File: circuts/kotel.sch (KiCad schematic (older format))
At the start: 21 parts, among them IC1 ATMEGA328P-TQFP32, P1 Power, P2 RELE CONNECTOR, P3 UART_RST, P4 TWI SW, Q1 MOS_N, U1 MAX6634, U2 7805, X1 12mHz

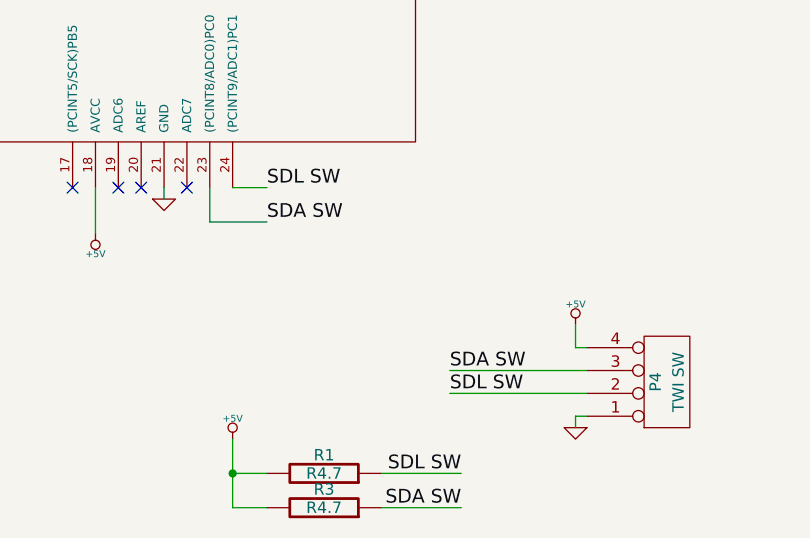
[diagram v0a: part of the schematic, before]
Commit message: Fixed software SDL/SCL.
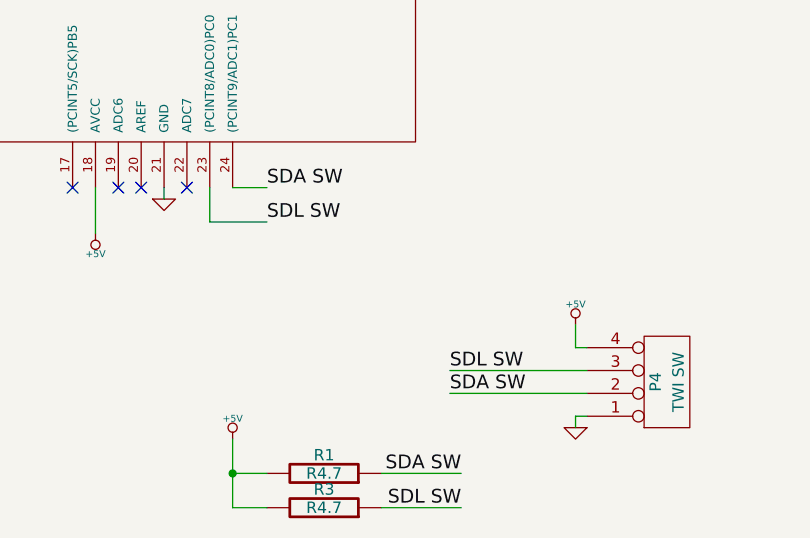
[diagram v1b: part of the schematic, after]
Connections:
- net SDA SW: now also IC1.24 ((PCINT9/ADC1)PC1), P4.2 (P2), R1.1; no longer IC1.23 ((PCINT8/ADC0)PC0), P4.3 (P3), R3.1
- net SDL SW: now also IC1.23 ((PCINT8/ADC0)PC0), P4.3 (P3), R3.1; no longer IC1.24 ((PCINT9/ADC1)PC1), P4.2 (P2), R1.1
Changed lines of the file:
@@
 Sheet 1 1
 Title "Humidity switcher"
-Date "26 sep 2013"
-Rev "v0.1"
+Date "6 oct 2013"
+Rev "v0.2"
 Comp ""
 Comment1 ""
@@
 $EndComp
 $Comp
-L GND #PWR018
+L GND #PWR017
 U 1 1 52360A3E
 P 6400 1550
-F 0 "#PWR018" H 6400 1550 30  0001 C CNN
+F 0 "#PWR017" H 6400 1550 30  0001 C CNN
 F 1 "GND" H 6400 1480 30  0001 C CNN
 F 2 "" H 6400 1550 60  0001 C CNN
@@
 $EndComp
 $Comp
-L GND #PWR019
+L GND #PWR018
 U 1 1 52360BDB
 P 2400 4950
-F 0 "#PWR019" H 2400 4950 30  0001 C CNN
+F 0 "#PWR018" H 2400 4950 30  0001 C CNN
 F 1 "GND" H 2400 4880 30  0001 C CNN
 F 2 "" H 2400 4950 60  0001 C CNN
@@
 $EndComp
 $Comp
-L +5V #PWR020
+L +5V #PWR019
 U 1 1 52360BE1
 P 2950 4400
-F 0 "#PWR020" H 2950 4490 20  0001 C CNN
+F 0 "#PWR019" H 2950 4490 20  0001 C CNN
 F 1 "+5V" H 2950 4490 30  0000 C CNN
 F 2 "" H 2950 4400 60  0000 C CNN
@@
 $EndComp
 $Comp
-L GND #PWR021
+L GND #PWR020
 U 1 1 52360C9E
 P 1750 4900
-F 0 "#PWR021" H 1750 4900 30  0001 C CNN
+F 0 "#PWR020" H 1750 4900 30  0001 C CNN
 F 1 "GND" H 1750 4830 30  0001 C CNN
 F 2 "" H 1750 4900 60  0001 C CNN
@@
 $EndComp
 $Comp
-L VCC #PWR022
+L VCC #PWR021
 U 1 1 52360D53
 P 1800 4300
-F 0 "#PWR022" H 1800 4400 30  0001 C CNN
+F 0 "#PWR021" H 1800 4400 30  0001 C CNN
 F 1 "VCC" H 1800 4400 30  0000 C CNN
 F 2 "" H 1800 4300 60  0000 C CNN
@@
 $EndComp
 $Comp
-L VCC #PWR023
+L VCC #PWR022
 U 1 1 52360DB8
 P 9050 1050
-F 0 "#PWR023" H 9050 1150 30  0001 C CNN
+F 0 "#PWR022" H 9050 1150 30  0001 C CNN
 F 1 "VCC" H 9050 1150 30  0000 C CNN
 F 2 "" H 9050 1050 60  0000 C CNN
@@
 $EndComp
 $Comp
-L GND #PWR024
+L GND #PWR023
 U 1 1 52361099
 P 2850 5000
-F 0 "#PWR024" H 2850 5000 30  0001 C CNN
+F 0 "#PWR023" H 2850 5000 30  0001 C CNN
 F 1 "GND" H 2850 4930 30  0001 C CNN
 F 2 "" H 2850 5000 60  0001 C CNN
@@
 $EndComp
 $Comp
-L GND #PWR025
+L GND #PWR024
 U 1 1 5236115C
 P 1950 5000
-F 0 "#PWR025" H 1950 5000 30  0001 C CNN
+F 0 "#PWR024" H 1950 5000 30  0001 C CNN
 F 1 "GND" H 1950 4930 30  0001 C CNN
 F 2 "" H 1950 5000 60  0001 C CNN
@@
 $EndComp
 $Comp
-L +5V #PWR026
+L +5V #PWR025
 U 1 1 52447FE3
 P 6950 4950
-F 0 "#PWR026" H 6950 5040 20  0001 C CNN
+F 0 "#PWR025" H 6950 5040 20  0001 C CNN
 F 1 "+5V" H 6950 5040 30  0000 C CNN
 F 2 "" H 6950 4950 60  0000 C CNN
@@
 $EndComp
 $Comp
-L GND #PWR027
+L GND #PWR026
 U 1 1 52447FE9
 P 6950 5400
-F 0 "#PWR027" H 6950 5400 30  0001 C CNN
+F 0 "#PWR026" H 6950 5400 30  0001 C CNN
 F 1 "GND" H 6950 5330 30  0001 C CNN
 F 2 "" H 6950 5400 60  0001 C CNN
@@
 Wire Wire Line
 	6950 5350 6950 5400
+Text Label 5600 4500 0    60   ~ 0
+SDL SW
 Text Label 5600 4350 0    60   ~ 0
+SDA SW
+Wire Wire Line
+	5450 4350 5600 4350
+Wire Wire Line
+	5600 4500 5350 4500
+Wire Wire Line
+	5350 4500 5350 4350
+Text Label 6400 5150 0    60   ~ 0
 SDL SW
-Text Label 5600 4500 0    60   ~ 0
-SDA SW
-Wire Wire Line
-	5450 4350 5600 4350
-Wire Wire Line
-	5600 4500 5350 4500
-Wire Wire Line
-	5350 4500 5350 4350
 Text Label 6400 5250 0    60   ~ 0
-SDL SW
-Text Label 6400 5150 0    60   ~ 0
 SDA SW
 Wire Wire Line
@@
 	0    1    -1   0
 $EndComp
+Text Label 6450 5600 2    60   ~ 0
+SDA SW
 Text Label 6450 5750 2    60   ~ 0
-SDA SW
-Text Label 6450 5600 2    60   ~ 0
 SDL SW
 $Comp
-L +5V #PWR028
+L +5V #PWR027
 U 1 1 52448436
 P 5450 5450
-F 0 "#PWR028" H 5450 5540 20  0001 C CNN
+F 0 "#PWR027" H 5450 5540 20  0001 C CNN
 F 1 "+5V" H 5450 5540 30  0000 C CNN
 F 2 "" H 5450 5450 60  0000 C CNN

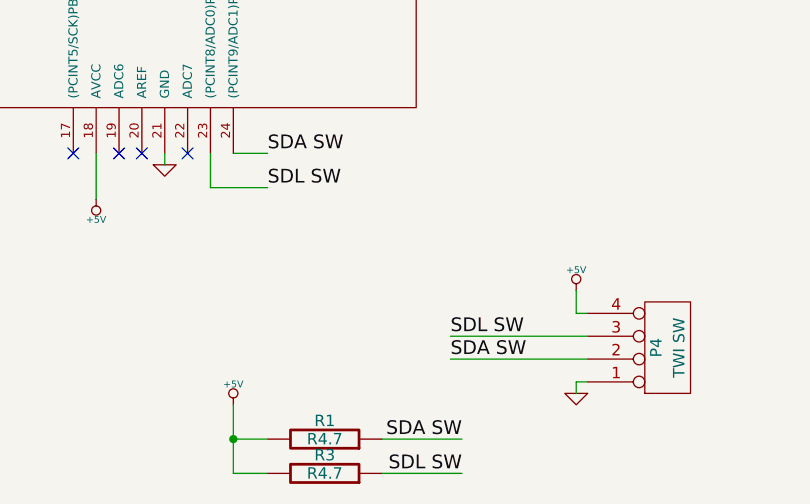
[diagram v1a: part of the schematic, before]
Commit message: Fixed name SDL to SCL.
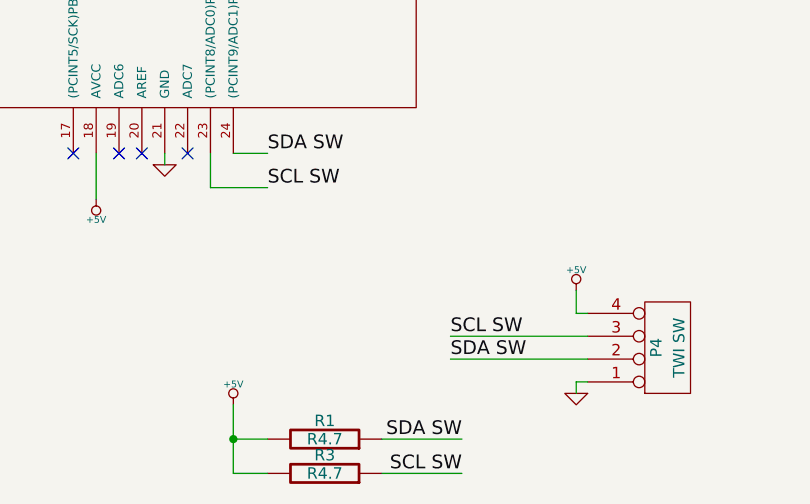
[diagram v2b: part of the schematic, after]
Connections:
- net SDL SW renamed SCL SW
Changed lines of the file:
@@
 	6950 5350 6950 5400
 Text Label 5600 4500 0    60   ~ 0
-SDL SW
+SCL SW
 Text Label 5600 4350 0    60   ~ 0
 SDA SW
@@
 	5350 4500 5350 4350
 Text Label 6400 5150 0    60   ~ 0
-SDL SW
+SCL SW
 Text Label 6400 5250 0    60   ~ 0
 SDA SW
@@
 SDA SW
 Text Label 6450 5750 2    60   ~ 0
-SDL SW
+SCL SW
 $Comp
 L +5V #PWR027
